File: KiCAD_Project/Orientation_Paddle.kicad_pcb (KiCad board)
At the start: 2 copper layers, 110.5 x 47 mm, 76 parts, among them J1 NP_Conn_01x04_Relief, J10 1-0000190, J2 1-0001205, J3 NP_Conn_01x03_Relief, J4 NP_Conn_01x02_Relief, J5 NP_Conn_01x02_Relief, J6 NP_Conn_01x04, J7 NP_Conn_01x04, J8 NP_Conn_01x02, J9 1-0000050, U1 1-0001232, U2 1-0001471, U3 1-0000207, U4 1-0000446, U5 1-0000785, Y1 1-0000721

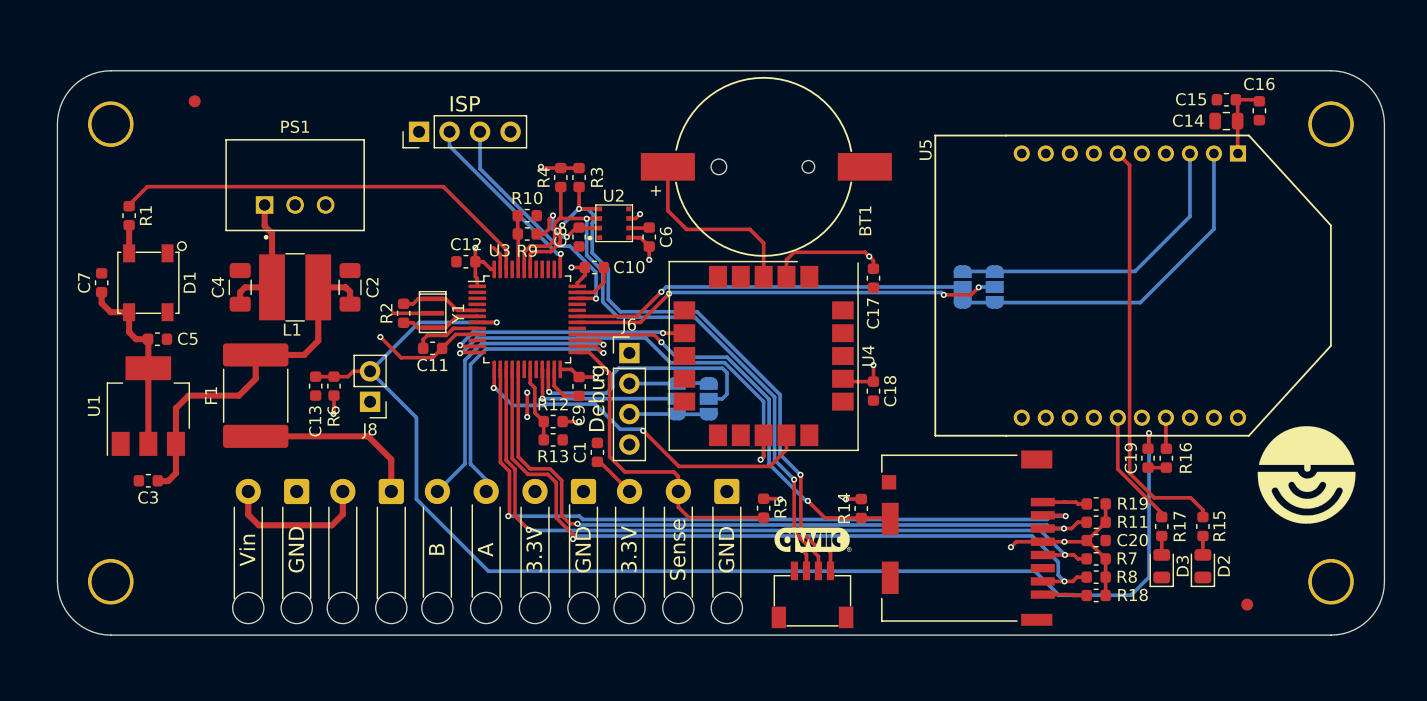
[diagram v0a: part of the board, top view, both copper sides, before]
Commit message: Rev 2.0 Changes: Fixed the following issues, - Issue #7 (Added RP Protection) - Issue #6 (Removed old encoder and sense connections) - Issue #5 (Solidified Serial connections by removing jumpers) - Issue #4 (Swapped GPS TX and RX) - Issue #3 (Removed old LED, add SMPL RGB LED) - Issue #2 (Labled ISCP Header) - Issue #1 (Changed DEBUG header to new SMPL DEBUG Connector) Other additions/changes: - Marked all XBEE Components as no pop - Updated board and rev numbers
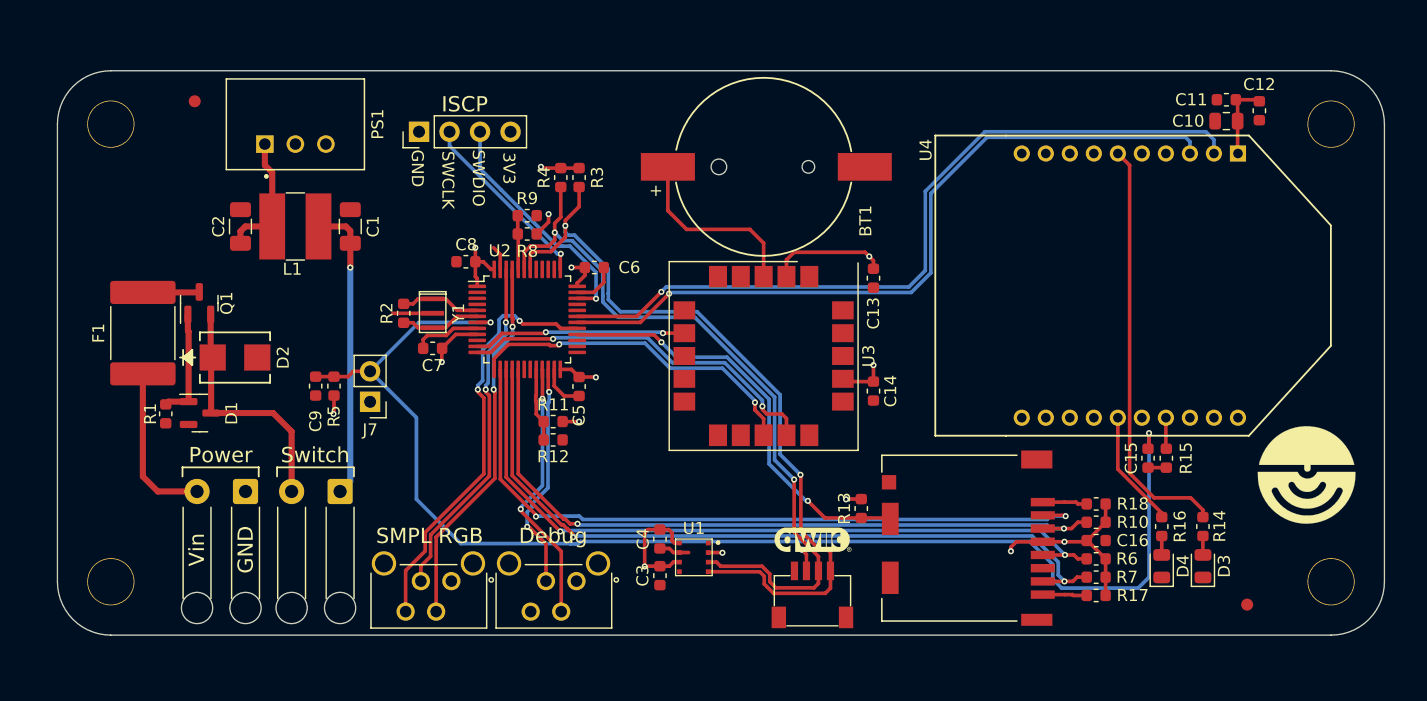
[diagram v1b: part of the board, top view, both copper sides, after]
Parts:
- removed the C1 at (116.7, 128.9)
- removed the C5 at (80.1, 119.5)
- removed the C6 at (121.0, 111.0)
- removed the C7 at (75.4, 114.8)
- removed the C8 at (115.2, 111.0)
- removed the J1 at (109.4, 130.6)
- removed the J7 at (101.9, 102.2)
- removed JP1, JP2, JP5, JP6: SolderJumper_3_Open, Jumper:SolderJumper-3_P1.3mm_Open_RoundedPad1.0x1.5mm_NumberLabels
- removed the R5 at (130.6, 133.6)
- removed the U2 at (118.1, 109.9)
- added C4: 1-0000007, capacitors_0603:1-0000007, F.Cu at (121.9, 136.1)
- added D2: 1-0001537, diodes:1-0001537, F.Cu at (86.5, 121.0)
- added J2: 1-0001156, connectors:1-0001156, F.Cu at (102.6, 138.2)
- added Q1: 1-0001670, mosfets:1-0001670, F.Cu at (83.6, 116.5)
- C3: value 1-0000018 -> 1-0000007; footprint capacitors_0603:1-0000018 -> capacitors_0603:1-0000007
- D1: value 1-0000399 -> 1-0001672; footprint leds_other:1-0000399 -> diodes:1-0001672
- J3: value NP_Conn_01x03_Relief -> 1-0001156; footprint np_connectors:SolderWire_1x03_Relief -> connectors:1-0001156
- R1: value 1-0000679 -> 1-0000174; footprint resistors_0603:1-0000679 -> resistors_0603:1-0000174
- U1: value 1-0001232 -> 1-0001471; footprint regulators:1-0001232 -> sensors:1-0001471
- moved U1 47.1 mm to (124.7, 137.7), turned to 0 degrees
- moved C3 43.3 mm to (121.9, 139.2), turned to 90 degrees
- moved J6 25.4 mm to (101.9, 102.2), turned to 90 degrees
- moved R1 16.8 mm to (80.8, 125.7)
- moved D1 11.7 mm to (83.6, 125.7), turned to 0 degrees
- moved J3 11.3 mm to (113.0, 138.2)
- moved F1 10.7 mm to (78.9, 119.0)
- moved PS1 5.07 mm to (91.6, 101.6)
- moved C1 5.07 mm to (96.1, 110.1)
- moved C2 5.07 mm to (87.0, 110.1)
- moved L1 5.07 mm to (91.6, 110.1)
- moved J4 4.26 mm to (85.3, 131.6)
- moved J5 4.26 mm to (93.2, 131.6)
- renumbered C2 to C1, C14 to C10, C15 to C11, C16 to C12, C17 to C13, C18 to C14, C19 to C15, C20 to C16, C4 to C2, C9 to C5, C10 to C6, C11 to C7, C12 to C8, C13 to C9, D2 to D3, D3 to D4, J2 to J1, J8 to J7, J9 to J8, J10 to J9, R11 to R10, R12 to R11, R13 to R12, R14 to R13, R15 to R14, R16 to R15, R17 to R16, R18 to R17, R19 to R18, R6 to R5, R7 to R6, R8 to R7, R9 to R8, R10 to R9, U3 to U2, U4 to U3, U5 to U4
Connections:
- C3 pad 1: +BATT -> GND
- C3 pad 2: GND -> +3V3
- D1 pad 1: +5V -> Net-(D1-A)
- D1 pad 3: GND -> Net-(D1-K)
- F1 pad 1: Net-(J5-Pin_1) -> Net-(J4-Pin_2)
- F1 pad 2: +BATT -> Net-(Q1-D)
- J3 pad 2: Mag_Sens -> UART3_TX
- J3 pad 3: +3V3 -> UART3_RX
- J5 pad 1: Net-(J5-Pin_1) -> +BATT
- J5 pad 2: Net-(J4-Pin_2) -> Net-(D1-K)
- J6 pad 2: UART3_TX -> SWCLK
- J6 pad 3: UART3_RX -> SWDIO
- R1 pad 1: LED -> Net-(D1-A)
- R1 pad 2: Net-(D1-DIN) -> GND
- U1 pad 2: +5V -> +3V3
- U1 pad 3: +BATT -> SDA
- U2 pad 12: GPS_TX -> GPS_RX
- U2 pad 13: GPS_RX -> GPS_TX
- U2 pad 19: Boot1 -> unconnected-(U2-PB1-Pad19)
- U2 pad 20: unconnected-(U3-PB2-Pad20) -> Boot1
- U2 pad 21: Net-(JP1-C) -> UART3_TX
- U2 pad 22: Net-(JP2-C) -> UART3_RX
- U2 pad 25: Mag_Sens -> unconnected-(U2-PB12-Pad25)
- U2 pad 26: Encoder_A -> unconnected-(U2-PB13-Pad26)
- U2 pad 27: Encoder_B -> unconnected-(U2-PB14-Pad27)
- U2 pad 29: unconnected-(U3-PA8-Pad29) -> Status_LED_B
- U2 pad 30: Net-(JP5-C) -> XBee_TX
- U2 pad 31: Net-(JP6-C) -> XBee_RX
- U2 pad 45: unconnected-(U3-PB8-Pad45) -> Status_LED_R
- U2 pad 46: LED -> Status_LED_G
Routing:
- net XBee_TX: track 26.1 -> 62.4 mm, vias 0 -> 1
- net Net-(JP5-C): track 36.1 -> 0.00 mm, vias 3 -> 0
- net LED: track 35.9 -> 0.00 mm
- net Status_LED_B: track 0.00 -> 35.0 mm, vias 0 -> 2
- net XBee_RX: track 29.7 -> 64.7 mm, vias 0 -> 1
- net Net-(JP6-C): track 33.1 -> 0.00 mm, vias 1 -> 0
- net Status_LED_R: track 0.00 -> 31.1 mm, vias 0 -> 2
- net Status_LED_G: track 0.00 -> 29.2 mm, vias 0 -> 2
- net Mag_Sens: track 26.8 -> 0.00 mm
- net Encoder_B: track 26.4 -> 0.00 mm, vias 1 -> 0
- net Encoder_A: track 25.3 -> 0.00 mm, vias 1 -> 0
- net Net-(JP2-C): track 21.9 -> 0.00 mm, vias 1 -> 0
- net Net-(D1-K): track 0.00 -> 20.7 mm
- net +5V: track 15.7 -> 0.00 mm
- net UART3_TX: track 6.62 -> 22.3 mm, vias 0 -> 2
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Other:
- board text added: "3-0000267"
- board text added: "3V3"
- board text added: "G"
- board text added: "ISCP"
- board text added: "Leeman Geophysical LLC Orientation Paddle PCB Rev 2.0"
- board text added: "R"
- board text added: "RX"
- board text added: "SMPL RGB"
- board text added: "SWCLK"
- board text added: "SWDIO"
- board text added: "TX"
- board text removed: "3-0000205"
- board text removed: "3.3V"
- board text removed: "A"
- board text removed: "Encoder"
- board text removed: "ISP"
- board text removed: "Leeman Geophysical LLC Orientation Paddle PCB Rev 1.0"
- board text removed: "Mag"
- board text removed: "Sense"

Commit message: Make Rev 2.0 production files
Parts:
- renumbered U4 to U3, U3 to U4
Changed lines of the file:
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@@
 			(outputformat 1)
 			(mirror no)
-			(drillshape 1)
+			(drillshape 0)
 			(scaleselection 1)
-			(outputdirectory "")
+			(outputdirectory "../Production/GERBERS/")
 		)
 	)
@@
 	(net 32 "Net-(U2-PD0)")
 	(net 33 "Net-(U2-PD1)")
-	(net 34 "Net-(U4-~{DIO10{slash}PWM0})")
+	(net 34 "Net-(U3-~{DIO10{slash}PWM0})")
 	(net 35 "Boot0")
 	(net 36 "Boot1")
-	(net 37 "Net-(U4-AD3{slash}DIO3{slash}nSSEL)")
-	(net 38 "Net-(U4-Assoc{slash}DIO5)")
+	(net 37 "Net-(U3-AD3{slash}DIO3{slash}nSSEL)")
+	(net 38 "Net-(U3-Assoc{slash}DIO5)")
 	(net 39 "unconnected-(U2-PB0-Pad18)")
 	(net 40 "unconnected-(U2-PB14-Pad27)")
@@
 	(net 55 "unconnected-(U2-PB4-Pad40)")
 	(net 56 "unconnected-(U2-PA15-Pad38)")
-	(net 57 "unconnected-(U3-~{SAFEBOOT}-Pad8)")
-	(net 58 "unconnected-(U3-SCL-Pad12)")
-	(net 59 "unconnected-(U3-SDA-Pad9)")
-	(net 60 "unconnected-(U3-~{RESET}-Pad18)")
-	(net 61 "unconnected-(U3-EXTINT-Pad19)")
-	(net 62 "unconnected-(U4-nCTS{slash}DIO7-Pad12)")
-	(net 63 "unconnected-(U4-DIO11{slash}PWM1-Pad7)")
-	(net 64 "unconnected-(U4-DIO3{slash}MOSI-Pad11)")
-	(net 65 "unconnected-(U4-AD2{slash}DIO2{slash}CLK-Pad18)")
-	(net 66 "unconnected-(U4-VREF-Pad14)")
-	(net 67 "unconnected-(U4-nSLEEP{slash}DIO9-Pad13)")
-	(net 68 "unconnected-(U4-AD1{slash}DIO1{slash}ATTN-Pad19)")
-	(net 69 "unconnected-(U4-nRTS{slash}DIO6-Pad16)")
-	(net 70 "unconnected-(U4-AD0{slash}DIO0-Pad20)")
-	(net 71 "unconnected-(U4-RSVD-Pad8)")
-	(net 72 "unconnected-(U4-DIO12{slash}MISO-Pad4)")
-	(net 73 "unconnected-(U4-nRESET-Pad5)")
-	(net 74 "unconnected-(U4-nDTR{slash}DIO8-Pad9)")
+	(net 57 "unconnected-(U3-nCTS{slash}DIO7-Pad12)")
+	(net 58 "unconnected-(U3-DIO11{slash}PWM1-Pad7)")
+	(net 59 "unconnected-(U3-DIO3{slash}MOSI-Pad11)")
+	(net 60 "unconnected-(U3-AD2{slash}DIO2{slash}CLK-Pad18)")
+	(net 61 "unconnected-(U3-VREF-Pad14)")
+	(net 62 "unconnected-(U3-nSLEEP{slash}DIO9-Pad13)")
+	(net 63 "unconnected-(U3-AD1{slash}DIO1{slash}ATTN-Pad19)")
+	(net 64 "unconnected-(U3-nRTS{slash}DIO6-Pad16)")
+	(net 65 "unconnected-(U3-AD0{slash}DIO0-Pad20)")
+	(net 66 "unconnected-(U3-RSVD-Pad8)")
+	(net 67 "unconnected-(U3-DIO12{slash}MISO-Pad4)")
+	(net 68 "unconnected-(U3-nRESET-Pad5)")
+	(net 69 "unconnected-(U3-nDTR{slash}DIO8-Pad9)")
+	(net 70 "unconnected-(U4-~{SAFEBOOT}-Pad8)")
+	(net 71 "unconnected-(U4-SCL-Pad12)")
+	(net 72 "unconnected-(U4-SDA-Pad9)")
+	(net 73 "unconnected-(U4-~{RESET}-Pad18)")
+	(net 74 "unconnected-(U4-EXTINT-Pad19)")
 	(footprint "resistors_0603:1-0000010"
 		(layer "F.Cu")
@@
 			(layers "F.Cu" "F.Mask" "F.Paste")
 			(roundrect_rratio 0.25)
-			(net 34 "Net-(U4-~{DIO10{slash}PWM0})")
+			(net 34 "Net-(U3-~{DIO10{slash}PWM0})")
 			(pintype "passive")
 		)
@@
 			(layers "F.Cu" "F.Mask" "F.Paste")
 			(roundrect_rratio 0.25)
-			(net 37 "Net-(U4-AD3{slash}DIO3{slash}nSSEL)")
+			(net 37 "Net-(U3-AD3{slash}DIO3{slash}nSSEL)")
 			(pintype "passive")
 		)
@@
 			)
 		)
-		(property "Populated" "1"
+		(property "Populated" "0"
 			(at 0 0 90)
 			(unlocked yes)
@@
 			(layers "F.Cu" "F.Mask" "F.Paste")
 			(roundrect_rratio 0.25)
-			(net 38 "Net-(U4-Assoc{slash}DIO5)")
+			(net 38 "Net-(U3-Assoc{slash}DIO5)")
 			(pintype "passive")
 		)
@@
 			)
 			(layer "F.SilkS")
-			(net 45)
 		)
 		(fp_line
@@
 			)
 			(layer "F.SilkS")
-			(net 45)
 		)
 		(fp_line
@@
 			)
 			(layer "F.SilkS")
-			(net 45)
 		)
 		(fp_line
@@
 			)
 			(layer "F.SilkS")
-			(net 45)
 		)
 		(fp_line
@@
 			)
 			(layer "F.SilkS")
-			(net 45)
 		)
 		(fp_line
@@
 			)
 			(layer "F.SilkS")
-			(net 45)
 		)
 		(fp_line
@@
 			)
 			(layer "F.CrtYd")
-			(net 45)
 		)
 		(fp_line
@@
 			)
 			(layer "F.CrtYd")
-			(net 45)
 		)
 		(fp_line
@@
 			)
 			(layer "F.CrtYd")
-			(net 45)
 		)
 		(fp_line
@@
 			)
 			(layer "F.CrtYd")
-			(net 45)
 		)
 		(fp_line
@@
 			)
 			(layer "F.Fab")
-			(net 45)
 		)
 		(fp_line
@@
 			)
 			(layer "F.Fab")
-			(net 45)
 		)
 		(fp_line
@@
 			)
 			(layer "F.Fab")
-			(net 45)
 		)
 		(fp_line
@@
 			)
 			(layer "F.Fab")
-			(net 45)
 		)
 		(fp_line
@@
 			)
 			(layer "F.Fab")
-			(net 45)
 		)
 		(fp_text user "${REFERENCE}"
@@
 		(descr "Through hole straight pin header, 2x10, 2.00mm pitch, double rows")
 		(tags "Through hole pin header THT 2x10 2.00mm double row")
-		(property "Reference" "U4"
+		(property "Reference" "U3"
 			(at -11.285 25.978 90)
 			(layer "F.SilkS")
@@
 			(layers "*.Cu" "*.Mask")
 			(remove_unused_layers no)
-			(net 72 "unconnected-(U4-DIO12{slash}MISO-Pad4)")
+			(net 67 "unconnected-(U3-DIO12{slash}MISO-Pad4)")
 			(pinfunction "DIO12/MISO")
 			(pintype "bidirectional+no_connect")
@@
 			(layers "*.Cu" "*.Mask")
 			(remove_unused_layers no)
-			(net 73 "unconnected-(U4-nRESET-Pad5)")
+			(net 68 "unconnected-(U3-nRESET-Pad5)")
 			(pinfunction "nRESET")
 			(pintype "input+no_connect")
@@
 			(layers "*.Cu" "*.Mask")
 			(remove_unused_layers no)
-			(net 34 "Net-(U4-~{DIO10{slash}PWM0})")
+			(net 34 "Net-(U3-~{DIO10{slash}PWM0})")
 			(pinfunction "~{DIO10/PWM0}")
 			(pintype "bidirectional")
@@
 			(layers "*.Cu" "*.Mask")
 			(remove_unused_layers no)
-			(net 63 "unconnected-(U4-DIO11{slash}PWM1-Pad7)")
+			(net 58 "unconnected-(U3-DIO11{slash}PWM1-Pad7)")
 			(pinfunction "DIO11/PWM1")
 			(pintype "bidirectional+no_connect")
@@
 			(layers "*.Cu" "*.Mask")
 			(remove_unused_layers no)
-			(net 71 "unconnected-(U4-RSVD-Pad8)")
+			(net 66 "unconnected-(U3-RSVD-Pad8)")
 			(pinfunction "RSVD")
 			(pintype "no_connect")
@@
 			(layers "*.Cu" "*.Mask")
 			(remove_unused_layers no)
-			(net 74 "unconnected-(U4-nDTR{slash}DIO8-Pad9)")
+			(net 69 "unconnected-(U3-nDTR{slash}DIO8-Pad9)")
 			(pinfunction "nDTR/DIO8")
 			(pintype "bidirectional+no_connect")
@@
 			(layers "*.Cu" "*.Mask")
 			(remove_unused_layers no)
-			(net 64 "unconnected-(U4-DIO3{slash}MOSI-Pad11)")
+			(net 59 "unconnected-(U3-DIO3{slash}MOSI-Pad11)")
 			(pinfunction "DIO3/MOSI")
 			(pintype "power_in+no_connect")
@@
 			(layers "*.Cu" "*.Mask")
 			(remove_unused_layers no)
-			(net 62 "unconnected-(U4-nCTS{slash}DIO7-Pad12)")
+			(net 57 "unconnected-(U3-nCTS{slash}DIO7-Pad12)")
 			(pinfunction "nCTS/DIO7")
 			(pintype "power_in+no_connect")
@@
 			(layers "*.Cu" "*.Mask")
 			(remove_unused_layers no)
-			(net 67 "unconnected-(U4-nSLEEP{slash}DIO9-Pad13)")
+			(net 62 "unconnected-(U3-nSLEEP{slash}DIO9-Pad13)")
 			(pinfunction "nSLEEP/DIO9")
 			(pintype "output+no_connect")
@@
 			(layers "*.Cu" "*.Mask")
 			(remove_unused_layers no)
-			(net 66 "unconnected-(U4-VREF-Pad14)")
+			(net 61 "unconnected-(U3-VREF-Pad14)")
 			(pinfunction "VREF")
 			(pintype "input+no_connect")
@@
 			(layers "*.Cu" "*.Mask")
 			(remove_unused_layers no)
-			(net 38 "Net-(U4-Assoc{slash}DIO5)")
+			(net 38 "Net-(U3-Assoc{slash}DIO5)")
 			(pinfunction "Assoc/DIO5")
 			(pintype "bidirectional")
@@
 			(layers "*.Cu" "*.Mask")
 			(remove_unused_layers no)
-			(net 69 "unconnected-(U4-nRTS{slash}DIO6-Pad16)")
+			(net 64 "unconnected-(U3-nRTS{slash}DIO6-Pad16)")
 			(pinfunction "nRTS/DIO6")
 			(pintype "bidirectional+no_connect")
@@
 			(layers "*.Cu" "*.Mask")
 			(remove_unused_layers no)
-			(net 37 "Net-(U4-AD3{slash}DIO3{slash}nSSEL)")
+			(net 37 "Net-(U3-AD3{slash}DIO3{slash}nSSEL)")
 			(pinfunction "AD3/DIO3/nSSEL")
 			(pintype "bidirectional")
@@
 			(layers "*.Cu" "*.Mask")
 			(remove_unused_layers no)
-			(net 65 "unconnected-(U4-AD2{slash}DIO2{slash}CLK-Pad18)")
+			(net 60 "unconnected-(U3-AD2{slash}DIO2{slash}CLK-Pad18)")
 			(pinfunction "AD2/DIO2/CLK")
 			(pintype "bidirectional+no_connect")
@@
 			(layers "*.Cu" "*.Mask")
 			(remove_unused_layers no)
-			(net 68 "unconnected-(U4-AD1{slash}DIO1{slash}ATTN-Pad19)")
+			(net 63 "unconnected-(U3-AD1{slash}DIO1{slash}ATTN-Pad19)")
 			(pinfunction "AD1/DIO1/ATTN")
 			(pintype "bidirectional+no_connect")
@@
 			(layers "*.Cu" "*.Mask")
 			(remove_unused_layers no)
-			(net 70 "unconnected-(U4-AD0{slash}DIO0-Pad20)")
+			(net 65 "unconnected-(U3-AD0{slash}DIO0-Pad20)")
 			(pinfunction "AD0/DIO0")
 			(pintype "bidirectional+no_connect")
@@
 			)
 		)
-		(property "Populated" "1"
+		(property "Populated" "0"
 			(at 0 0 0)
 			(unlocked yes)
@@
 		(descr "GPS Module, 15.5x15.5x6.3mm, https://www.u-blox.com/sites/default/files/SAM-M8Q_HardwareIntegrationManual_%28UBX-16018358%29.pdf")
 		(tags "ublox SAM-M8Q")
-		(property "Reference" "U3"
+		(property "Reference" "U4"
 			(at 0 -8.75 90)
 			(layer "F.SilkS")
@@
 			(size 1.5 1.8)
 			(layers "F.Cu" "F.Mask")
-			(net 57 "unconnected-(U3-~{SAFEBOOT}-Pad8)")
+			(net 70 "unconnected-(U4-~{SAFEBOOT}-Pad8)")
 			(pinfunction "~{SAFEBOOT}")
 			(pintype "input+no_connect")
@@
 			(size 1.5 1.8)
 			(layers "F.Cu" "F.Mask")
-			(net 59 "unconnected-(U3-SDA-Pad9)")
+			(net 72 "unconnected-(U4-SDA-Pad9)")
 			(pinfunction "SDA")
 			(pintype "bidirectional+no_connect")
@@
 			(size 1.8 1.5)
 			(layers "F.Cu" "F.Mask")
-			(net 58 "unconnected-(U3-SCL-Pad12)")
+			(net 71 "unconnected-(U4-SCL-Pad12)")
 			(pinfunction "SCL")
 			(pintype "input+no_connect")
@@
 			(size 1.5 1.8)
 			(layers "F.Cu" "F.Mask")
-			(net 60 "unconnected-(U3-~{RESET}-Pad18)")
+			(net 73 "unconnected-(U4-~{RESET}-Pad18)")
 			(pinfunction "~{RESET}")
 			(pintype "input+no_connect")
@@
 			(size 1.5 1.8)
 			(layers "F.Cu" "F.Mask")
-			(net 61 "unconnected-(U3-EXTINT-Pad19)")
+			(net 74 "unconnected-(U4-EXTINT-Pad19)")
 			(pinfunction "EXTINT")
 			(pintype "input+no_connect")
@@
 			)
 		)
-		(property "Populated" "1"
+		(property "Populated" "0"
 			(at 0 0 270)
 			(unlocked yes)
